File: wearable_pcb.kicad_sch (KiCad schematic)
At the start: 0 parts

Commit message: first class with pcb
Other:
- added sheet micro (micro.kicad_sch)
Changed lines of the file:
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@@
 	(generator "eeschema")
 	(generator_version "9.0")
-	(paper "A4")
+	(paper "A3")
+	(sheet
+		(at 40.64 34.29)
+		(size 48.26 39.37)
+		(exclude_from_sim no)
+		(in_bom yes)
+		(on_board yes)
+		(dnp no)
+		(fields_autoplaced yes)
+		(stroke
+			(width 0.1524)
+			(type solid)
+		)
+		(fill
+			(color 0 0 0 0.0000)
+		)
+		(property "Sheetname" "micro"
+			(at 40.64 33.5784 0)
+			(effects
+				(font
+					(size 1.27 1.27)
+				)
+				(justify left bottom)
+			)
+		)
+		(property "Sheetfile" "micro.kicad_sch"
+			(at 40.64 74.2446 0)
+			(effects
+				(font
+					(size 1.27 1.27)
+				)
+				(justify left top)
+			)
+		)
+		(instances
+			(project "wearable_pcb"
+				(path "/f8be0e19-e585-4ec4-900a-ea71de23765b"
+					(page "2")
+				)
+			)
+		)
+	)
 	(sheet_instances
 		(path "/"

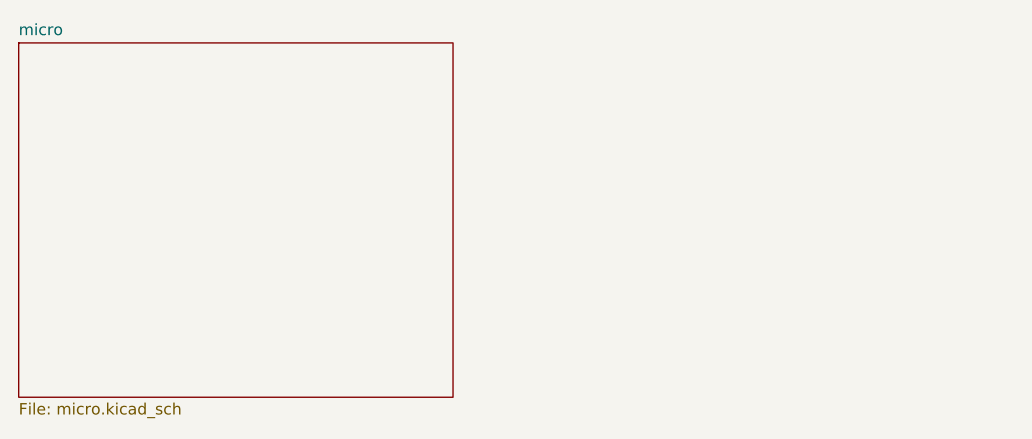
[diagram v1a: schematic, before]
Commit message: ultimas dos clases - anyadidas mas footprints mas esquematico
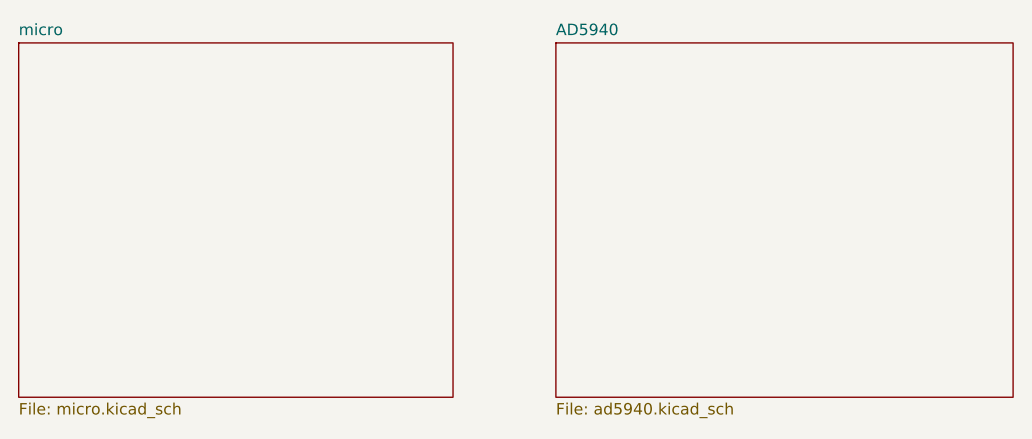
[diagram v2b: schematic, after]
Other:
- added sheet AD5940 (ad5940.kicad_sch)
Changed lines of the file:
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@@
+		)
+	)
+	(sheet
+		(at 100.33 34.29)
+		(size 50.8 39.37)
+		(exclude_from_sim no)
+		(in_bom yes)
+		(on_board yes)
+		(dnp no)
+		(fields_autoplaced yes)
+		(stroke
+			(width 0.1524)
+			(type solid)
+		)
+		(fill
+			(color 0 0 0 0.0000)
+		)
+		(property "Sheetname" "AD5940"
+			(at 100.33 33.5784 0)
+			(effects
+				(font
+					(size 1.27 1.27)
+				)
+				(justify left bottom)
+			)
+		)
+		(property "Sheetfile" "ad5940.kicad_sch"
+			(at 100.33 74.2446 0)
+			(effects
+				(font
+					(size 1.27 1.27)
+				)
+				(justify left top)
+			)
+		)
+		(property "Field2" ""
+			(at 100.33 34.29 0)
+			(effects
+				(font
+					(size 1.27 1.27)
+				)
+			)
+		)
+		(instances
+			(project "wearable_pcb"
+				(path "/f8be0e19-e585-4ec4-900a-ea71de23765b"
+					(page "3")
+				)
+			)
 		)
 	)
